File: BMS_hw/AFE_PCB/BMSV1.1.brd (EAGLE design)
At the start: 272 x 60 mm, 272 parts, among them IC1 MC33771BEP, IC2 SFH6156-1, IC3 MIC28515V1, IC4 FOD8384-COC, IC5 FOD8384-COC, IC6 FOD8384-COC, IC7 SFH6156-1, IC8 SFH6156-1, Q1 IRLML5203, Q2 IRLML5203, T1 IPT020N10N3V1, T2 IPT020N10N3V1, T3 IPT020N10N3V1, T4 IPT020N10N3V1, U1 NCP1117LP-PG, U2 NCP1117LP-PG, X5 22-23-2041

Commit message: itt@21
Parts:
- moved C88 21.6 mm to (243.8, 27.3), turned to 270 degrees
- moved R85 20.7 mm to (247.0, 33.7), turned to 270 degrees
- moved R80 19.9 mm to (257.8, 33.0), turned to 270 degrees
- moved R82 19.3 mm to (259.7, 33.0), turned to 270 degrees
- moved R108 17.8 mm to (255.9, 33.0), turned to 270 degrees
- moved C86 17.3 mm to (241.9, 22.2), turned to 270 degrees
- moved C89 13.7 mm to (241.9, 27.3), turned to 90 degrees
- moved C85 12.7 mm to (268.0, 11.4), turned to 0 degrees
- moved C66 12.5 mm to (245.7, 29.8)
- moved C83 11.4 mm to (268.0, 3.81), turned to 0 degrees
- moved C87 11.2 mm to (263.5, 3.81), turned to 0 degrees
- moved C64 10.4 mm to (247.0, 16.5), turned to 0 degrees
- moved R91 10.2 mm to (253.4, 31.7), turned to 270 degrees
- moved C84 9.92 mm to (268.0, 7.62), turned to 0 degrees
- moved C80 9.38 mm to (242.6, 17.1)
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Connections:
- net CB_14+/14_C: now also C63.2, C64.2, C80.2, C86.2, IC3.10, IC3.11, IC3.5, IC3.6, IC3.7, IC3.8, IC3.9, R79.1
- net VIN: no longer C63.2, C64.2, C80.2, C86.2, IC3.10, IC3.11, IC3.5, IC3.6, IC3.7, IC3.8, IC3.9, R79.1
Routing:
- net FB: track 81.0 -> 12.7 mm, vias 4 -> 0
- net CB_14+/14_C: track 296.2 -> 353.3 mm, vias 4 -> 9
- net SW: track 62.3 -> 11.2 mm, vias 3 -> 7
- net VIN: track 50.4 -> 0.00 mm, vias 2 -> 0
- net N$24: track 30.5 -> 0.00 mm
- net GND: track 117.6 -> 91.7 mm, vias 155 -> 132
- net VCC: track 39.2 -> 61.8 mm, vias 0 -> 3
- net N$21: track 36.6 -> 14.0 mm
- net PVDD: track 18.3 -> 4.71 mm, vias 3 -> 0
- net N$17: track 9.45 -> 0.00 mm
- net ILIM: track 9.36 -> 1.90 mm
- net N$12: track 4.76 -> 0.00 mm
- net VDD: track 4.69 -> 7.98 mm, vias 0 -> 2
- net N$13: track 2.47 -> 0.00 mm
- net CANH: track 85.0 -> 87.0 mm
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- added copper zone on layer 1, net CB_14+/14_C
- added copper zone on layer 16, net CB_14+/14_C
- added copper zone on layer 16, net SW

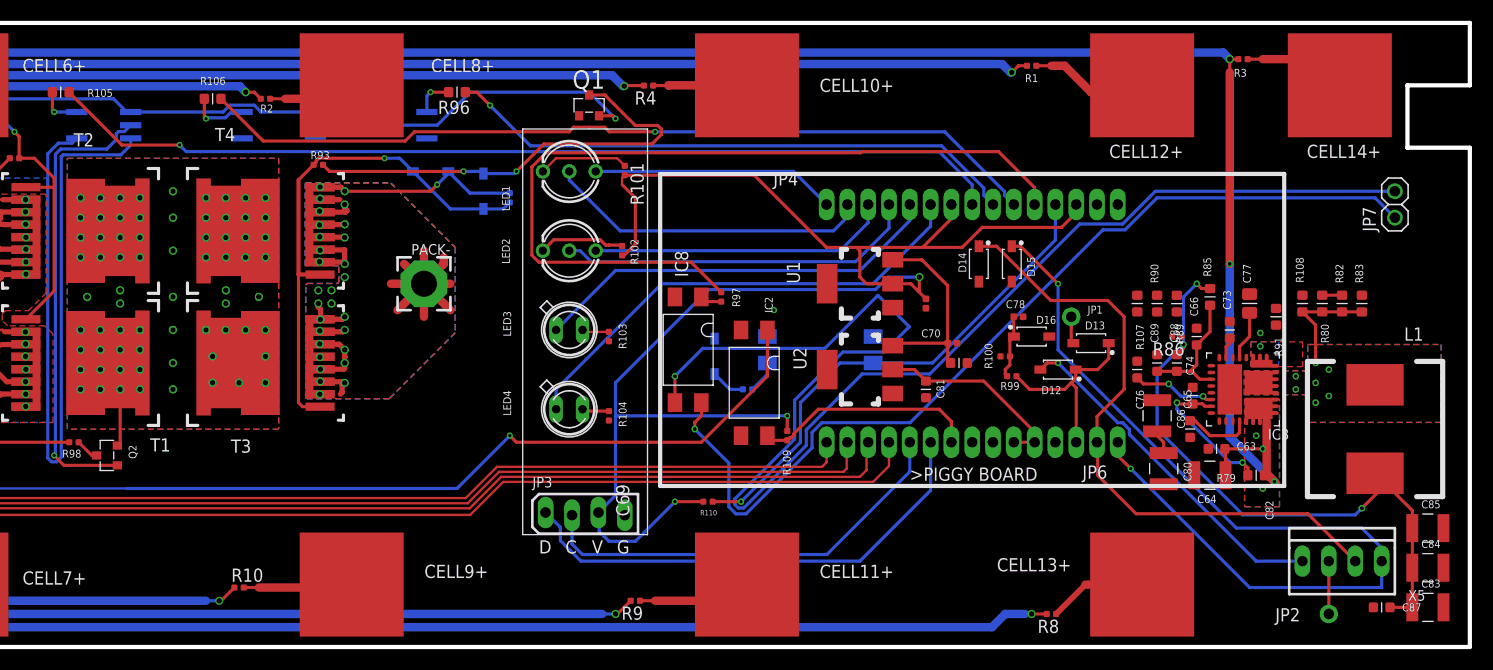
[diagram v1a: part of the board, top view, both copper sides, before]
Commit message: updated sch with diff AFE version1.1
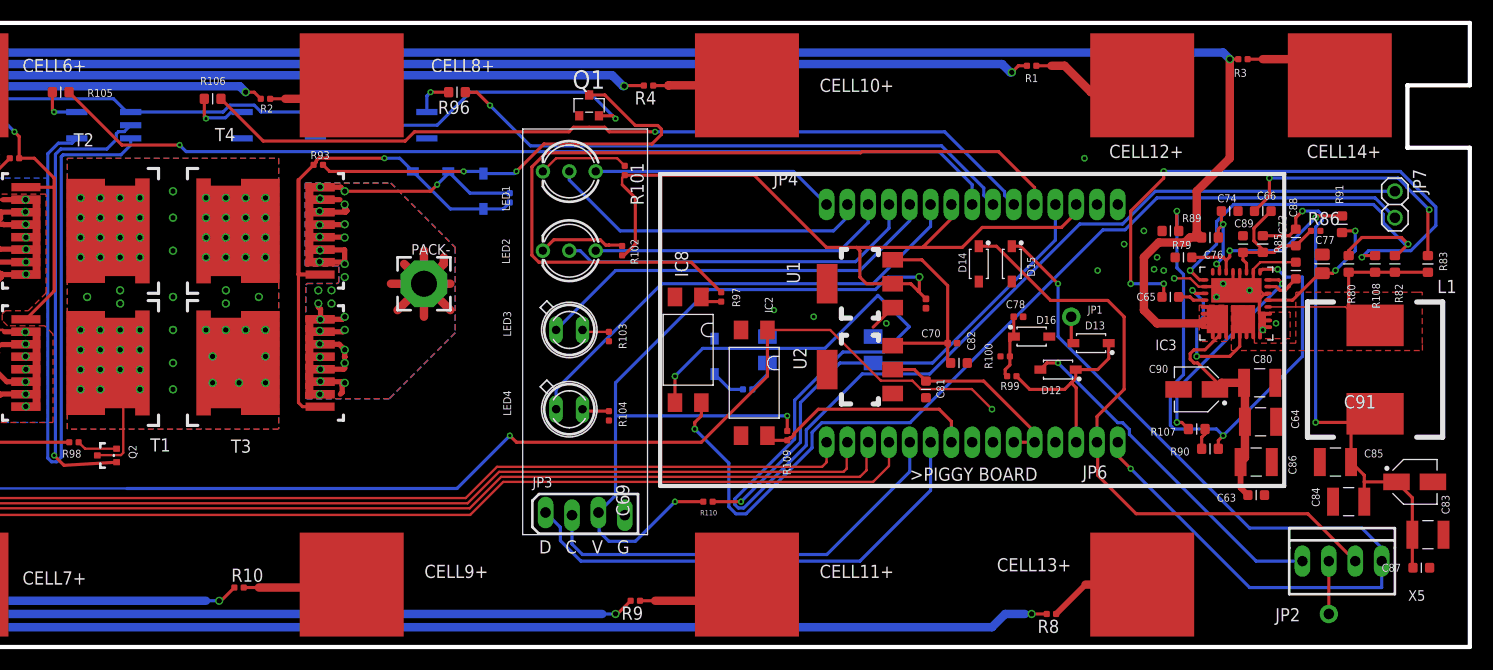
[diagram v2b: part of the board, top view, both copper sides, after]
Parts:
- added C90: 39uF 100V, ipc-7351-capacitor:CAPAE430X540N
- added C91: 330uF 25V, ipc-7351-capacitor:CAPAE430X540N
- Q2: value IRLML5203 -> BSS138PW; device transistor-power:MICRO3 -> simpa:SOT323
- R101, R102, R103, R104: value 10k -> 330E
- R98: value 10k -> 300E
- moved R79 23.3 mm to (247.0, 39.4), turned to 0 degrees
- moved C74 18.1 mm to (248.9, 41.9), turned to 0 degrees
- moved R86 16.8 mm to (257.2, 40.0), turned to 0 degrees
- moved C88 16.6 mm to (255.3, 39.4)
- moved R90 14.9 mm to (247.0, 19.1), turned to 180 degrees
- moved C89 14.1 mm to (250.2, 38.7)
- moved C66 13.6 mm to (252.1, 41.9), turned to 0 degrees
- moved R107 13.4 mm to (245.7, 21.0), turned to 0 degrees
- moved C65 12.8 mm to (243.2, 33.7), turned to 180 degrees
- moved C80 12.4 mm to (251.8, 25.4), turned to 180 degrees
- moved C76 11.7 mm to (244.5, 37.5), turned to 180 degrees
- moved R91 10.9 mm to (259.7, 40.6), turned to 90 degrees
- moved C85 10.9 mm to (259.1, 17.8), turned to 180 degrees
- moved C86 10.5 mm to (251.5, 17.8), turned to 180 degrees
- moved C84 9.92 mm to (260.4, 14.0), turned to 180 degrees
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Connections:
- removed net SGNL: D21.A
- net CB_14+/14_C: now also C90.+, IC7.2
- net GND: now also C90.-, C91.-, D21.A; no longer IC7.2
- net N$28: now also Q2.2; no longer Q2.3
- net PWR_DRAIN: now also Q2.3; no longer Q2.2
- net VCC: now also C91.+
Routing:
- net N$13: track 0.00 -> 55.7 mm, vias 0 -> 4
- net N$17: track 0.00 -> 53.2 mm, vias 0 -> 3
- net ILIM: track 1.90 -> 37.4 mm, vias 0 -> 2
- net GND: track 91.7 -> 118.8 mm, vias 132 -> 145
- net SW: track 11.2 -> 36.2 mm, vias 7 -> 2
- net N$24: track 0.00 -> 24.9 mm, vias 0 -> 2
- net N$31: track 119.7 -> 144.5 mm, vias 2 -> 3
- net N$12: track 0.00 -> 20.5 mm, vias 0 -> 2
- net VDD: track 7.98 -> 17.8 mm
- net PVDD: track 4.71 -> 13.6 mm, vias 0 -> 2
- net PWR_DRAIN: track 5.51 -> 12.7 mm, vias 70 -> 69
- net N$21: track 14.0 -> 7.75 mm
- net VCC: track 61.8 -> 56.7 mm, vias 3 -> 2
- net BST: track 6.56 -> 2.63 mm
- net CB_14+/14_C: track 353.3 -> 355.6 mm, vias 9 -> 4
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- removed copper zone on layer 16, net CB_14+/14_C
- removed copper zone on layer 16, net SW

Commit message: replace part with fod8384 with tlp152 added datasheet in doc folder
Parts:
- removed C80, C86: 2.2uF 100V, ipc-7351-capacitor:CAPC3225X168N
- added Q3, Q4, Q5, Q6, Q7, Q8: (no value), ipc-7351-transistor:SOT95P280X135-3N
- added R111, R112, R113, R114, R115: 330E, ipc-7351-resistor:RESC1005X40AN
- added R116, R117: 33E, ipc-7351-resistor:RESC1005X40AN
- added R118: 0E, ipc-7351-resistor:RESC1005X40AN
- C66: value 47nF -> 0.1uF 100V
- C73: value 1uF -> 2.2uF 16V
- C78: device ipc-7351-capacitor:CAPC1005X60N -> ipc-7351-capacitor:CAPC1608X92N
- C81, C82: device ipc-7351-capacitor:CAPC1608X92N -> ipc-7351-capacitor:CAPC1005X60N
- D16: device ipc-7351-diode:SOD3718X135N -> ipc-7351-diode:SOD2514X100N
- R101, R102: value 330E -> 33E
- R66: value 10 -> 10R; device ipc-7351-resistor:RESC1005X40AN -> ipc-7351-resistor:RESC1608X55N
- R7: value 100 -> 39E
- R79: value 127E -> 2E
- R80: value 1.6k -> 330E; device ipc-7351-resistor:RESC1608X55N -> ipc-7351-resistor:RESC1005X40AN
- moved R101 245.1 mm to (-41.3, -33.0), turned to 0 degrees
- moved R102 244.0 mm to (-41.3, -38.1), turned to 0 degrees
- moved R80 64.1 mm to (196.8, 45.7), flipped to the bottom, turned to 180 degrees
- moved JP2 17.3 mm to (268.6, 17.1)
- moved C87 13.5 mm to (258.4, 17.8), turned to 0 degrees
- moved C91 13.0 mm to (257.8, 6.35), turned to 180 degrees
- moved C83 10.2 mm to (257.8, 10.8), turned to 180 degrees
- moved C84 8.64 mm to (252.1, 11.4)
- moved X5 6.63 mm to (266.1, 10.2), turned to 90 degrees
- moved C85 3.42 mm to (257.8, 14.6)
- moved D21 3.18 mm to (202.6, 27.9)
- moved R103 2.84 mm to (188.0, 27.3), flipped to the bottom
- moved R95 2.54 mm to (205.1, 24.8)
- moved IC7 2.54 mm to (212.1, 28.6)
- moved R104 2.01 mm to (189.9, 24.1), flipped to the bottom, turned to 180 degrees
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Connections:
- removed net N$71: LED1.1, R101.1
- removed net N$74: LED2.1, R102.1
- new net N$22: Q7.3, R103.2
- new net N$29: Q8.3, R104.2
- new net N$32: Q3.1, R80.1
- new net N$37: Q4.1, R111.1
- new net N$39: Q6.1, R112.1
- new net N$40: Q5.1, R113.1
- new net N$42: Q7.1, R114.1
- new net N$43: Q8.1, R115.1
- new net N$44: LED1.3, R116.1
- new net N$45: Q3.3, R116.2
- new net N$47: LED1.1, R117.1
- new net N$56: Q6.3, R102.2
- new net N$57: Q5.3, R101.2
- new net N$58: Q4.3, R117.2
- new net N$59: LED2.3, R102.1
- new net N$60: LED2.1, R101.1
- new net N$61: IC3.26, R118.1
- net 3.3V: now also LED1.2, LED2.2, LED3.A, LED4.A; no longer R101.2, R102.2
- net CB_14+/14_C: no longer C80.2, C86.2
- net GND: now also Q3.2, Q4.2, Q5.2, Q6.2, Q7.2, Q8.2, R118.2; no longer C80.1, C86.1, IC3.26, R103.2, R104.2
- net ILIM: no longer R80.1
- net KEY-IN: no longer JP6.13
- net S-LED_1: now also R80.2; no longer LED1.3
- net S-LED_2: now also R111.2; no longer LED1.2
- net S-LED_3: now also R112.2; no longer LED2.3
- net S-LED_4: now also R113.2; no longer LED2.2
- net S-LED_5: now also R114.2; no longer LED3.A
- net S-LED_6: now also R115.2; no longer LED4.A
- net SW: no longer R80.2
- net WAKE: now also JP6.13
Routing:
- net N$15: track 133.0 -> 81.7 mm, vias 1 -> 3
- net CB_14+/14_C: track 355.6 -> 400.0 mm, vias 4 -> 8
- net CANH: track 86.3 -> 55.2 mm
- net INTL_IN2: track 33.6 -> 54.5 mm
- net S-LED_6: track 46.5 -> 65.9 mm, vias 0 -> 2
- net S-LED_2: track 31.3 -> 17.4 mm
- net VCC: track 56.7 -> 43.9 mm, vias 2 -> 4
- net GND: track 118.8 -> 131.1 mm, vias 145 -> 147
- net N$29: track 0.00 -> 11.9 mm, vias 0 -> 2
- net S-LED_5: track 39.9 -> 28.8 mm
- net N$43: track 0.00 -> 11.0 mm
- net S-LED_4: track 34.8 -> 24.1 mm
- net S-LED_1: track 23.5 -> 14.2 mm
- net S-LED_3: track 29.1 -> 20.0 mm
- net N$71: track 8.70 -> 0.00 mm
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- added copper zone on layer 1, net VCC
- removed copper zone on layer 16, net BGND
- removed copper zone on layer 16, net PWR_DRAIN

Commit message: afe and piggy board bom layout and schematic all changed for final only dc-dc convertor replacement required !
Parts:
- removed IC4, IC5, IC6: FOD8384-COC, GreenFuel:SOP5
- added IC10, IC11, IC9: TLP152-COUPLERTOSHIBA, GreenFuel:SO6-5PIN
- moved R118 309.8 mm to (255.9, 44.5)
- moved R102 245.2 mm to (191.8, 38.1)
- moved R116 242.5 mm to (191.1, 46.4)
- moved R101 232.2 mm to (180.3, 36.2), turned to 270 degrees
- moved R117 231.9 mm to (179.7, 42.5), turned to 270 degrees
- moved R97 3.70 mm to (198.1, 36.8)
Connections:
- net +15V: now also IC10.6, IC11.6, IC9.6; no longer IC4.6, IC5.6, IC6.6
- net CHG_FET: now also IC10.5; no longer IC5.5
- net DSG_FET: now also IC9.5; no longer IC4.5
- net GND: now also IC10.3, IC10.4, IC11.3, IC11.4, IC9.3, IC9.4; no longer IC4.3, IC4.4, IC5.3, IC5.4, IC6.3, IC6.4
- net N$20: now also IC9.1; no longer IC4.1
- net N$33: now also IC10.1; no longer IC5.1
- net N$35: now also IC11.1; no longer IC6.1
- net PCHG_FET: now also IC11.5; no longer IC6.5
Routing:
- net GND: track 131.1 -> 58.2 mm
- net SGNL1: track 80.2 -> 43.9 mm
- net N$57: track 1.39 -> 14.8 mm, vias 0 -> 1
- net N$58: track 0.00 -> 12.4 mm, vias 0 -> 1
- net WAKE: track 6.71 -> 18.2 mm
- net N$61: track 0.00 -> 10.2 mm, vias 0 -> 2
- net +15V: track 35.3 -> 39.9 mm
- net N$45: track 0.00 -> 4.61 mm, vias 0 -> 1
- net N$56: track 0.75 -> 5.11 mm, vias 0 -> 1
- net N$47: track 0.00 -> 4.30 mm
- net DSG_FET: track 29.6 -> 33.9 mm
- net N$20: track 4.15 -> 7.99 mm
- net CB_14+/14_C: track 400.0 -> 403.8 mm
- net N$33: track 3.79 -> 7.37 mm
- net VDD: track 17.8 -> 21.3 mm
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
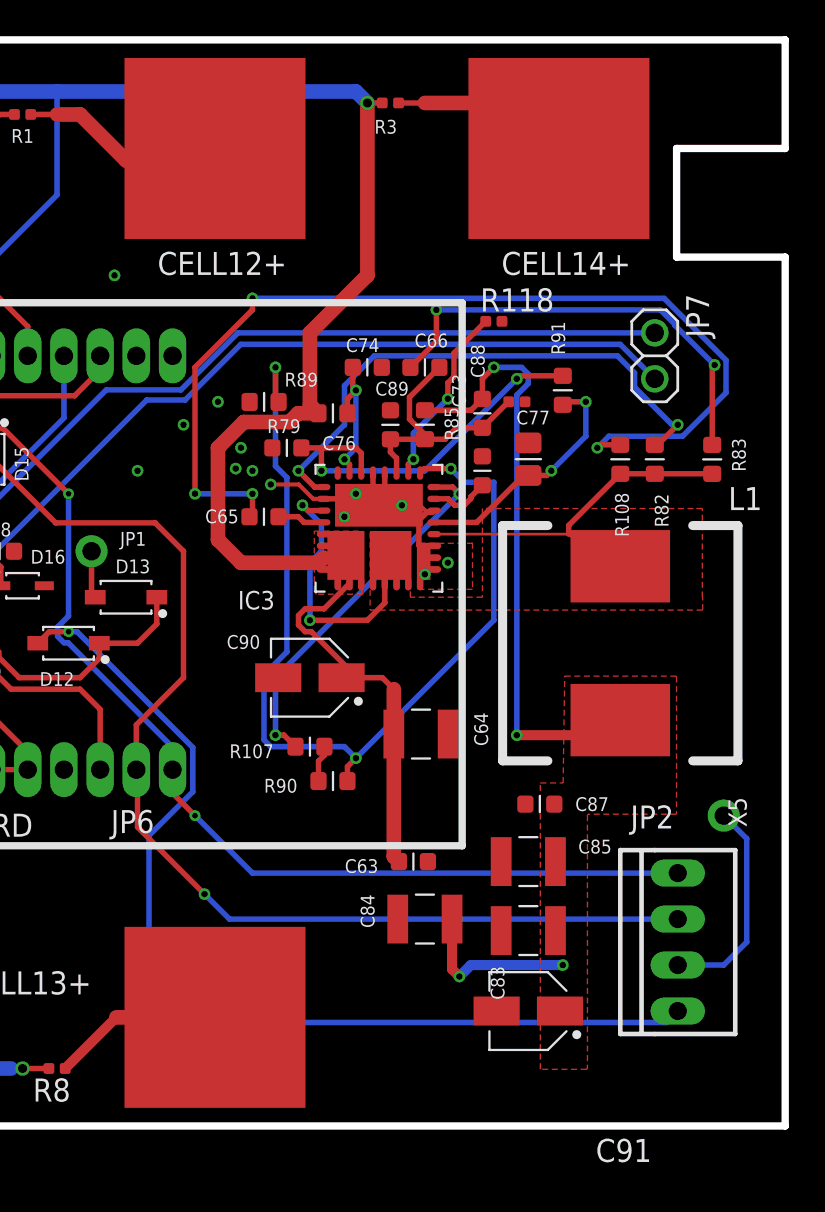
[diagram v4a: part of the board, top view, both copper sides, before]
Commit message: Afe board updated dc dc convertor
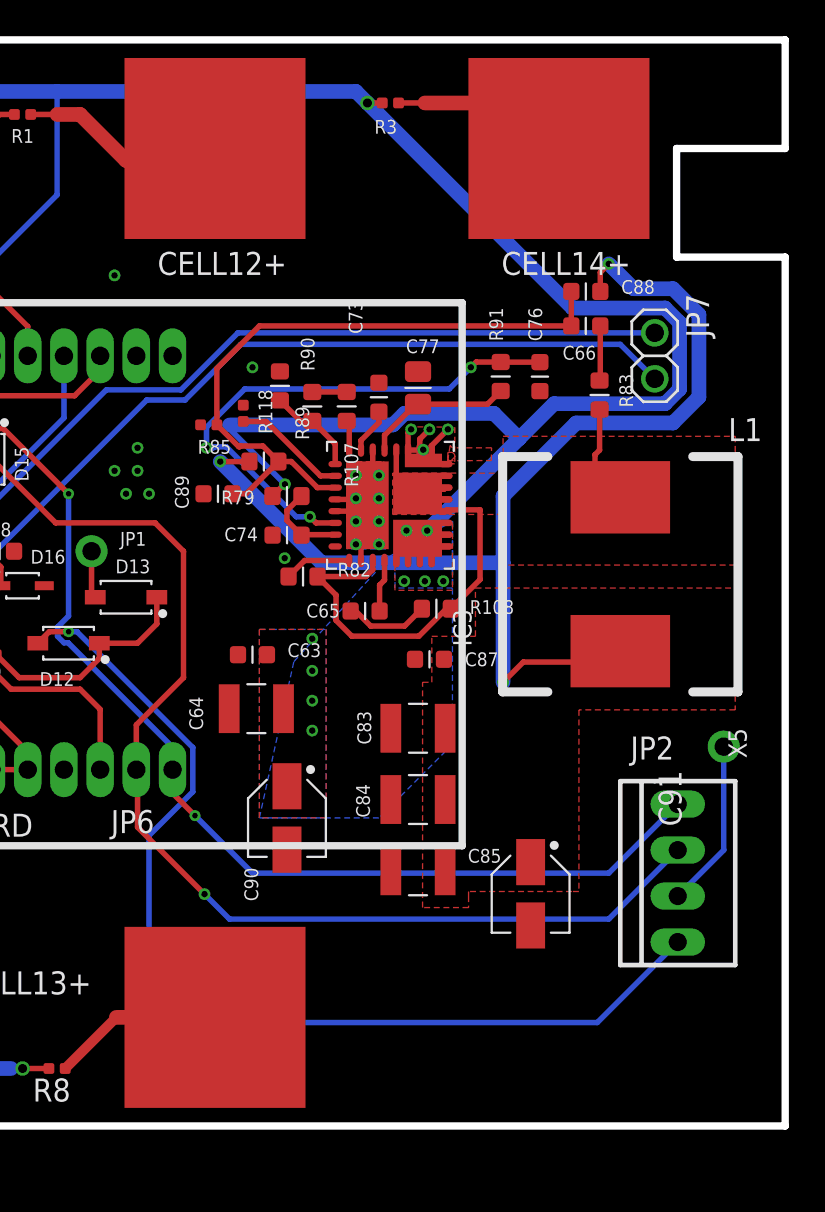
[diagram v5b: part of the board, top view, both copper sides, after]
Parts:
- moved R90 20.7 mm to (245.9, 39.7), turned to 90 degrees
- moved R82 20.5 mm to (245.4, 30.4), turned to 0 degrees
- moved R107 18.9 mm to (247.8, 39.8), turned to 90 degrees
- moved R86 17.1 mm to (240.2, 38.7), turned to 180 degrees
- moved R118 14.7 mm to (242.1, 39.4), turned to 90 degrees
- moved C76 14.5 mm to (258.4, 41.4), turned to 270 degrees
- moved C63 14.5 mm to (242.6, 26.0), turned to 0 degrees
- moved R108 13.1 mm to (252.7, 28.6), turned to 0 degrees
- moved C83 12.7 mm to (251.7, 22.0)
- moved C74 10.3 mm to (244.5, 32.6), turned to 180 degrees
- moved C89 10.3 mm to (240.7, 34.9), turned to 180 degrees
- moved C87 10.1 mm to (252.3, 25.8)
- moved C64 9.20 mm to (242.8, 23.1), turned to 0 degrees
- moved C66 9.18 mm to (261.0, 44.2), turned to 180 degrees
- moved R85 9.13 mm to (243.2, 36.7), turned to 0 degrees
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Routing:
- net N$13: track 55.7 -> 4.68 mm, vias 4 -> 0
- net N$17: track 53.2 -> 5.17 mm, vias 3 -> 0
- net ILIM: track 30.4 -> 3.72 mm, vias 2 -> 0
- net FB: track 14.4 -> 36.8 mm
- net N$24: track 24.9 -> 3.03 mm, vias 2 -> 0
- net N$12: track 20.5 -> 1.75 mm, vias 2 -> 0
- net VCC: track 43.9 -> 60.8 mm, vias 4 -> 3
- net VDD: track 21.3 -> 29.9 mm, vias 2 -> 3
- net CB_14+/14_C: track 403.8 -> 411.4 mm, vias 8 -> 18
- net PVDD: track 13.6 -> 8.25 mm, vias 2 -> 0
- net N$61: track 10.2 -> 6.32 mm, vias 2 -> 0
- net N$21: track 7.75 -> 4.69 mm, vias 2 -> 0
- net INTL_OUT1: track 11.8 -> 9.31 mm
- net SW: track 34.6 -> 32.3 mm, vias 2 -> 0
- net INTL_IN2: track 54.5 -> 56.1 mm
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- added copper zone on layer 16, net CB_14+/14_C

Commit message: AFE master bom itt, layout itt, sch itt
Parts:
- added R119: 127E, ipc-7351-resistor:RESC1005X40AN
- moved R34 98.0 mm to (10.2, 47.0), turned to 270 degrees
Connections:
- removed net +15V: IC10.6, IC11.6, IC9.6
- removed net 15V_AUX: C70.2, C82.2, U1.3, U2.3
- removed net VCC: C83.1, C84.1, C85.1, C87.2, C88.1, C91.+, L1.2, R85.1
- new net +12V: C70.2, C82.2, C83.1, C84.1, C85.1, C87.2, C88.1, C91.+, IC10.6, IC11.6, IC9.6, L1.2, R85.1, U1.3, U2.3
- net CB_14+/14_C: now also R119.1; no longer IC7.2
- net GND: no longer D21.A
- net N$25: now also IC7.2; no longer IC7.1
- net N$36: now also D21.A, R119.2; no longer D21.K
- net V+: now also D21.K, IC7.1
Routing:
- net +12V: track 0.00 -> 253.6 mm, vias 0 -> 6
- net VCC: track 60.8 -> 0.00 mm, vias 3 -> 0
- net V+: track 78.1 -> 135.2 mm, vias 30 -> 32
- net +15V: track 39.9 -> 0.00 mm
- net BGND: track 73.7 -> 39.2 mm
- net 15V_AUX: track 19.6 -> 0.00 mm
- net N$36: track 2.69 -> 13.9 mm, vias 0 -> 2
- net N$25: track 3.11 -> 8.84 mm, vias 0 -> 2
- net GND: track 58.7 -> 58.8 mm, vias 154 -> 155
- added copper zone on layer 1, net +12V
- removed copper zone on layer 1, net VCC

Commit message: afe board layout and schematic alt!
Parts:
- R1, R10, R2, R3, R32, R33, R36, R37, R38, R4, R41, R42, R43, R8, R9: value (none) -> 0E
- R34: value 0R -> 0E
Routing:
- net +12V: track 253.6 -> 249.7 mm
- net BGND: track 39.2 -> 36.0 mm

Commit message: 4.04mm space released from componrnrts for slidding!
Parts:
- added BGND@1: (no value), simpa:WPAD
- moved R8 3.81 mm to (231.8, 6.99)
- moved R1 3.24 mm to (230.5, 52.7)
- moved R3 3.24 mm to (250.8, 53.3)
- moved R9 1.27 mm to (191.8, 5.71)
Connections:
- net BGND: now also BGND@1.1
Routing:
- net BGND: track 36.0 -> 47.8 mm
- net CB_14+/14_C: track 411.5 -> 414.4 mm
- net CB_14/13_C: track 360.6 -> 363.5 mm
- net CB_13/12_C: track 326.3 -> 328.0 mm
- net CELL14+: track 9.90 -> 8.50 mm
- net CB_12/11_C: track 347.7 -> 348.9 mm
- net CELL12+: track 11.5 -> 10.6 mm
- net CELL13+: track 9.45 -> 8.68 mm
- net CELL11+: track 10.9 -> 10.4 mm
